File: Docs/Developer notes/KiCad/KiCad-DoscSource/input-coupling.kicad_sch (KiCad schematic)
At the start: 3 parts, among them J1 Conn_Coaxial, SW1 SW_SP3T

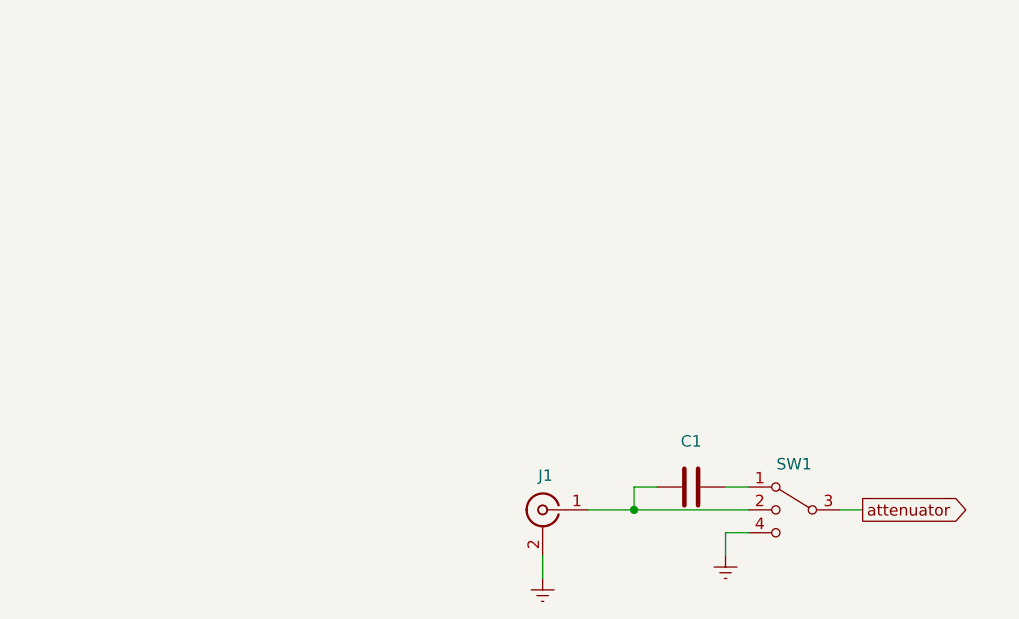
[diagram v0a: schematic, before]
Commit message: Add attenuator to developer notes
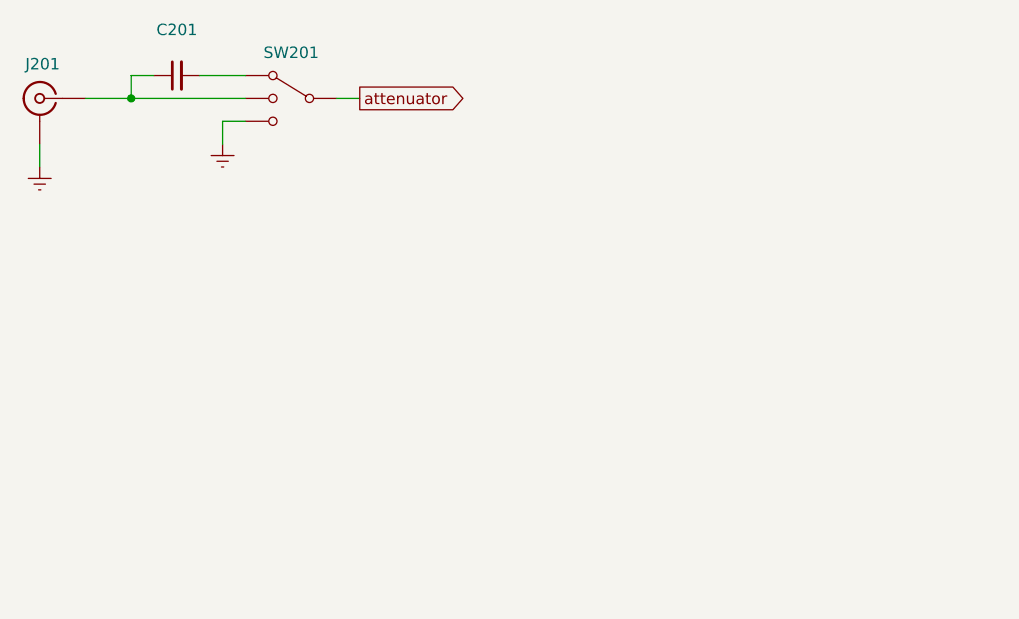
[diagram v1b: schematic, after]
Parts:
- C201: renamed from C1; symbol Device:C -> Device:C_Small
- renumbered J1 to J201, SW1 to SW201
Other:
- moved on the sheet: C201
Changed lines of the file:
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@@
 (kicad_sch (version 20230121) (generator eeschema)
-  (paper "A5")
-  (junction (at 71.12 55.88) (diameter 0) (color 0 0 0 0)
+  (paper "User" 54.991 25.4)
+  (junction (at 15.24 10.16) (diameter 0) (color 0 0 0 0)
   )
-  (wire (pts (xy 66.04 55.88) (xy 71.12 55.88))
+  (wire (pts (xy 10.16 10.16) (xy 15.24 10.16))
     (stroke (width 0) (type default))
   )
-  (wire (pts (xy 93.98 55.88) (xy 96.52 55.88))
+  (wire (pts (xy 38.1 10.16) (xy 40.64 10.16))
     (stroke (width 0) (type default))
   )
-  (wire (pts (xy 81.28 60.96) (xy 81.28 58.42))
+  (wire (pts (xy 25.4 15.24) (xy 25.4 12.7))
     (stroke (width 0) (type default))
   )
-  (wire (pts (xy 71.12 55.88) (xy 83.82 55.88))
+  (wire (pts (xy 15.24 10.16) (xy 27.94 10.16))
     (stroke (width 0) (type default))
   )
-  (wire (pts (xy 71.12 53.34) (xy 73.66 53.34))
+  (wire (pts (xy 25.4 12.7) (xy 27.94 12.7))
     (stroke (width 0) (type default))
   )
-  (wire (pts (xy 81.28 58.42) (xy 83.82 58.42))
+  (wire (pts (xy 15.24 7.62) (xy 15.24 10.16))
     (stroke (width 0) (type default))
   )
-  (wire (pts (xy 71.12 53.34) (xy 71.12 55.88))
+  (wire (pts (xy 5.08 15.24) (xy 5.08 17.78))
     (stroke (width 0) (type default))
   )
-  (wire (pts (xy 60.96 60.96) (xy 60.96 63.5))
+  (wire (pts (xy 22.86 7.62) (xy 27.94 7.62))
     (stroke (width 0) (type default))
   )
-  (wire (pts (xy 81.28 53.34) (xy 83.82 53.34))
+  (wire (pts (xy 15.24 7.62) (xy 17.78 7.62))
     (stroke (width 0) (type default))
   )
-  (global_label "attenuator" (shape output) (at 96.52 55.88 0) (fields_autoplaced)
+  (global_label "attenuator" (shape output) (at 40.64 10.16 0) (fields_autoplaced)
     (effects (font (size 1.27 1.27)) (justify left))
-    (property "Intersheetrefs" "${INTERSHEET_REFS}" (at 109.3021 55.88 0)
+    (property "Intersheetrefs" "${INTERSHEET_REFS}" (at 53.4221 10.16 0)
       (effects (font (size 1.27 1.27)) (justify left) hide)
     )
   )
-  (symbol (lib_id "Switch:SW_SP3T") (at 88.9 55.88 0) (mirror y) (unit 1)
+  (symbol (lib_id "Switch:SW_SP3T") (at 33.02 10.16 0) (mirror y) (unit 1)
     (in_bom yes) (on_board yes) (dnp no)
-    (property "Reference" "SW1" (at 88.9 50.8 0)
+    (property "Reference" "SW201" (at 33.02 5.08 0)
       (effects (font (size 1.27 1.27)))
     )
-    (property "Value" "SW_SP3T" (at 88.9 50.8 0)
+    (property "Value" "SW_SP3T" (at 33.02 5.08 0)
       (effects (font (size 1.27 1.27)) hide)
     )
-    (property "Footprint" "" (at 104.775 51.435 0)
+    (property "Footprint" "" (at 48.895 5.715 0)
       (effects (font (size 1.27 1.27)) hide)
     )
-    (property "Datasheet" "~" (at 104.775 51.435 0)
+    (property "Datasheet" "~" (at 48.895 5.715 0)
       (effects (font (size 1.27 1.27)) hide)
     )
@@
       (project "KiCad-DoscSource"
         (path "/1d440e8f-b221-47d3-bac2-5e91222a75a8/e6ea977f-63d3-4e66-b5a3-7108384f1d4c"
-          (reference "SW1") (unit 1)
+          (reference "SW201") (unit 1)
+        )
+        (path "/1d440e8f-b221-47d3-bac2-5e91222a75a8/328369cc-943c-47ea-a4b7-34fe34797705"
+          (reference "SW2") (unit 1)
         )
       )
     )
   )
-  (symbol (lib_id "power:Earth") (at 60.96 63.5 0) (unit 1)
+  (symbol (lib_id "power:Earth") (at 5.08 17.78 0) (unit 1)
     (in_bom yes) (on_board yes) (dnp no) (fields_autoplaced)
-    (property "Reference" "#PWR01" (at 60.96 69.85 0)
+    (property "Reference" "#PWR0201" (at 5.08 24.13 0)
       (effects (font (size 1.27 1.27)) hide)
     )
-    (property "Value" "Earth" (at 60.96 67.31 0)
+    (property "Value" "Earth" (at 5.08 21.59 0)
       (effects (font (size 1.27 1.27)) hide)
     )
-    (property "Footprint" "" (at 60.96 63.5 0)
+    (property "Footprint" "" (at 5.08 17.78 0)
       (effects (font (size 1.27 1.27)) hide)
     )
-    (property "Datasheet" "~" (at 60.96 63.5 0)
+    (property "Datasheet" "~" (at 5.08 17.78 0)
       (effects (font (size 1.27 1.27)) hide)
     )
@@
       (project "KiCad-DoscSource"
         (path "/1d440e8f-b221-47d3-bac2-5e91222a75a8/e6ea977f-63d3-4e66-b5a3-7108384f1d4c"
-          (reference "#PWR01") (unit 1)
+          (reference "#PWR0201") (unit 1)
+        )
+        (path "/1d440e8f-b221-47d3-bac2-5e91222a75a8/328369cc-943c-47ea-a4b7-34fe34797705"
+          (reference "#PWR04") (unit 1)
         )
       )
     )
   )
-  (symbol (lib_id "Device:C") (at 77.47 53.34 90) (unit 1)
+  (symbol (lib_id "Device:C_Small") (at 20.32 7.62 90) (unit 1)
     (in_bom yes) (on_board yes) (dnp no)
-    (property "Reference" "C1" (at 77.47 48.26 90)
+    (property "Reference" "C201" (at 20.32 2.54 90)
       (effects (font (size 1.27 1.27)))
     )
-    (property "Value" "C" (at 77.47 48.26 90)
+    (property "Value" "C" (at 20.32 2.54 90)
       (effects (font (size 1.27 1.27)) hide)
     )
-    (property "Footprint" "" (at 81.28 52.3748 0)
+    (property "Footprint" "" (at 20.32 7.62 0)
       (effects (font (size 1.27 1.27)) hide)
     )
-    (property "Datasheet" "~" (at 77.47 53.34 0)
+    (property "Datasheet" "~" (at 20.32 7.62 0)
       (effects (font (size 1.27 1.27)) hide)
     )
@@
       (project "KiCad-DoscSource"
         (path "/1d440e8f-b221-47d3-bac2-5e91222a75a8/e6ea977f-63d3-4e66-b5a3-7108384f1d4c"
-          (reference "C1") (unit 1)
+          (reference "C201") (unit 1)
+        )
+        (path "/1d440e8f-b221-47d3-bac2-5e91222a75a8/328369cc-943c-47ea-a4b7-34fe34797705"
+          (reference "C2") (unit 1)
         )
       )
     )
   )
-  (symbol (lib_id "Connector:Conn_Coaxial") (at 60.96 55.88 0) (mirror y) (unit 1)
+  (symbol (lib_id "Connector:Conn_Coaxial") (at 5.08 10.16 0) (mirror y) (unit 1)
     (in_bom yes) (on_board yes) (dnp no)
-    (property "Reference" "J1" (at 61.2774 52.07 0)
+    (property "Reference" "J201" (at 5.3974 6.35 0)
       (effects (font (size 1.27 1.27)))
     )
-    (property "Value" "Conn_Coaxial" (at 61.2774 52.07 0)
+    (property "Value" "Conn_Coaxial" (at 5.3974 6.35 0)
       (effects (font (size 1.27 1.27)) hide)
     )
-    (property "Footprint" "" (at 60.96 55.88 0)
+    (property "Footprint" "" (at 5.08 10.16 0)
       (effects (font (size 1.27 1.27)) hide)
     )
-    (property "Datasheet" " ~" (at 60.96 55.88 0)
+    (property "Datasheet" " ~" (at 5.08 10.16 0)
       (effects (font (size 1.27 1.27)) hide)
     )
@@
       (project "KiCad-DoscSource"
         (path "/1d440e8f-b221-47d3-bac2-5e91222a75a8/e6ea977f-63d3-4e66-b5a3-7108384f1d4c"
-          (reference "J1") (unit 1)
+          (reference "J201") (unit 1)
+        )
+        (path "/1d440e8f-b221-47d3-bac2-5e91222a75a8/328369cc-943c-47ea-a4b7-34fe34797705"
+          (reference "J2") (unit 1)
         )
       )
     )
   )
-  (symbol (lib_id "power:Earth") (at 81.28 60.96 0) (unit 1)
+  (symbol (lib_id "power:Earth") (at 25.4 15.24 0) (unit 1)
     (in_bom yes) (on_board yes) (dnp no) (fields_autoplaced)
-    (property "Reference" "#PWR02" (at 81.28 67.31 0)
+    (property "Reference" "#PWR0202" (at 25.4 21.59 0)
       (effects (font (size 1.27 1.27)) hide)
     )
-    (property "Value" "Earth" (at 81.28 64.77 0)
+    (property "Value" "Earth" (at 25.4 19.05 0)
       (effects (font (size 1.27 1.27)) hide)
     )
-    (property "Footprint" "" (at 81.28 60.96 0)
+    (property "Footprint" "" (at 25.4 15.24 0)
       (effects (font (size 1.27 1.27)) hide)
     )
-    (property "Datasheet" "~" (at 81.28 60.96 0)
+    (property "Datasheet" "~" (at 25.4 15.24 0)
       (effects (font (size 1.27 1.27)) hide)
     )
@@
       (project "KiCad-DoscSource"
         (path "/1d440e8f-b221-47d3-bac2-5e91222a75a8/e6ea977f-63d3-4e66-b5a3-7108384f1d4c"
-          (reference "#PWR02") (unit 1)
+          (reference "#PWR0202") (unit 1)
+        )
+        (path "/1d440e8f-b221-47d3-bac2-5e91222a75a8/328369cc-943c-47ea-a4b7-34fe34797705"
+          (reference "#PWR03") (unit 1)
         )
       )
